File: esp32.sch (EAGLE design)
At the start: 65 parts, among them IC1 PEC11R-4230K-S00243D, IC2 AD8532ARZ, T1 BST82-1, T2 BST82-1, T3 BST82-1, U1 ESP32-WROOM-32D, X1 JST-XH-02-PIN-LONG-PAD, X2 JST-XH-03-PIN-LONG-PAD, X3 JST-XH-03-PIN-LONG-PAD, X4 JST-XH-02-PIN-LONG-PAD

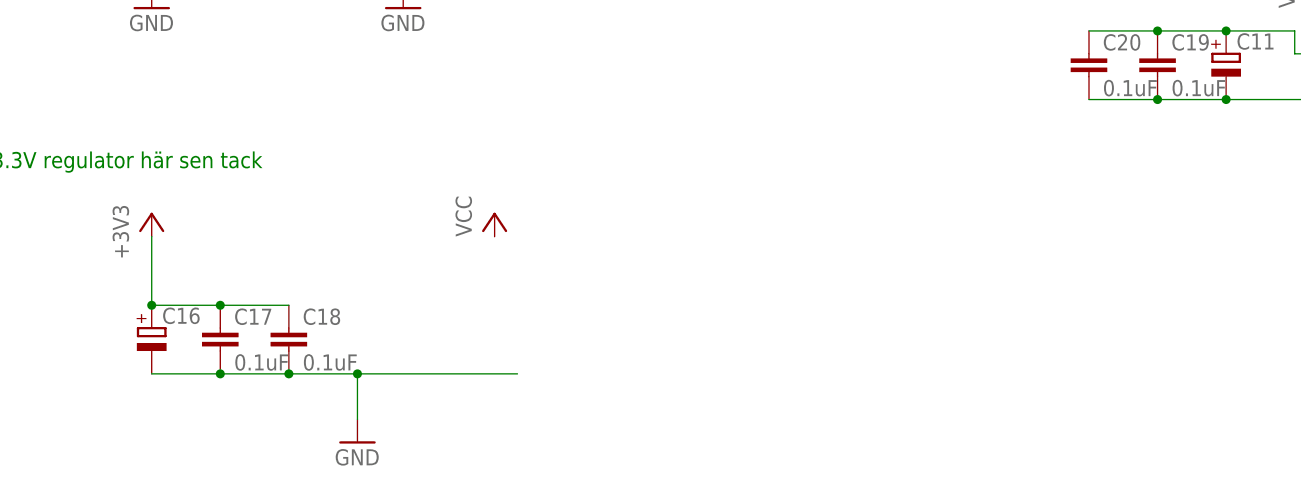
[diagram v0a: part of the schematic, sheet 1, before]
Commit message: Delade upp i lite olika plan. Rätta footprints för kondingar och 3.3V regulator.
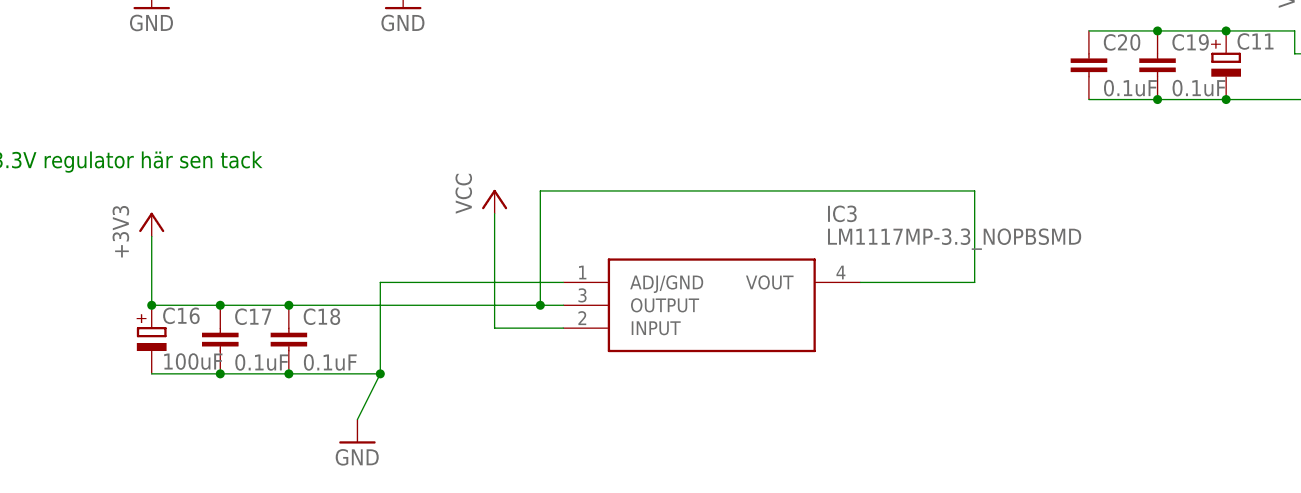
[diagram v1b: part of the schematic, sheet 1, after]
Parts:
- added IC3: LM1117MP-3.3_NOPBSMD, Test:LM1117MP-3.3_NOPBSMD
- C11, C14, C22: device rcl:CPOL-EU140CLH-0810 -> rcl:CPOL-EU153CLV-0605
- C16: value (none) -> 100uF; device rcl:CPOL-EU140CLH-0810 -> rcl:CPOL-EU153CLV-0605
- C7, C8: device rcl:C-EUC0603 -> rcl:CPOL-EU153CLV-0505
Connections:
- net +3V3: now also IC3.OUTPUT, IC3.VOUT
- net AUDIO_FROM_ESP32: now also C8.+; no longer C8.1
- net GND: now also C7.-, IC3.ADJ/GND; no longer C7.2
- net N$10: now also C7.+; no longer C7.1
- net N$4: now also C8.-; no longer C8.2
- net VCC: now also IC3.INPUT

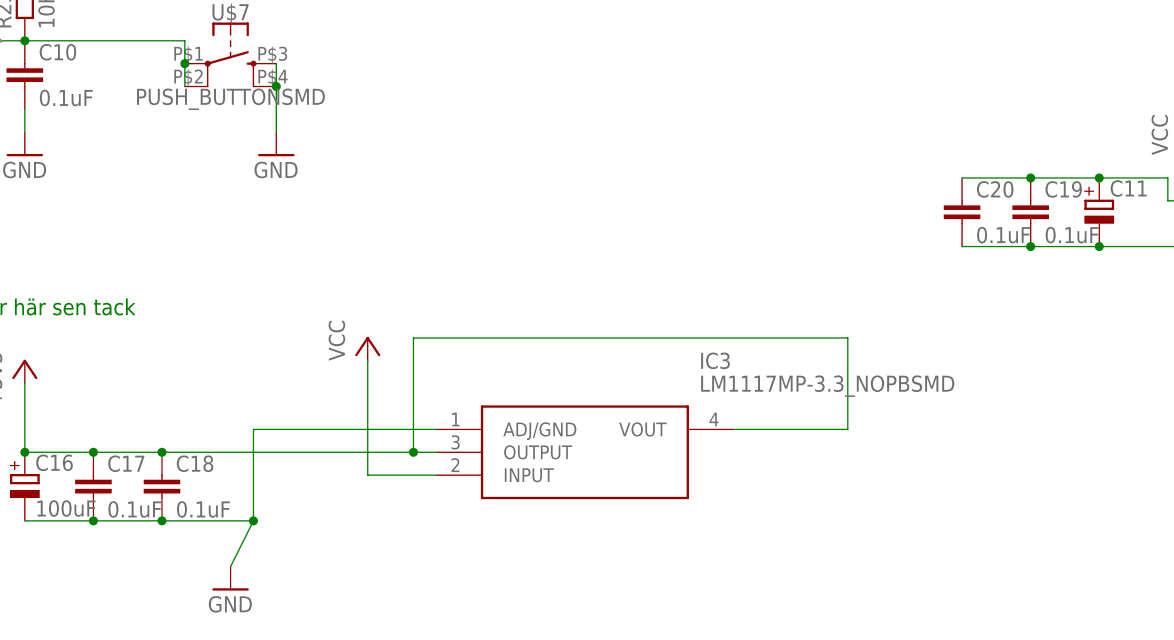
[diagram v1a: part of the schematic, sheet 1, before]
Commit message: Delad upp jordplanet till flera beroende på signal, hört att det ska vara bra att ta bort loopar i jorden.
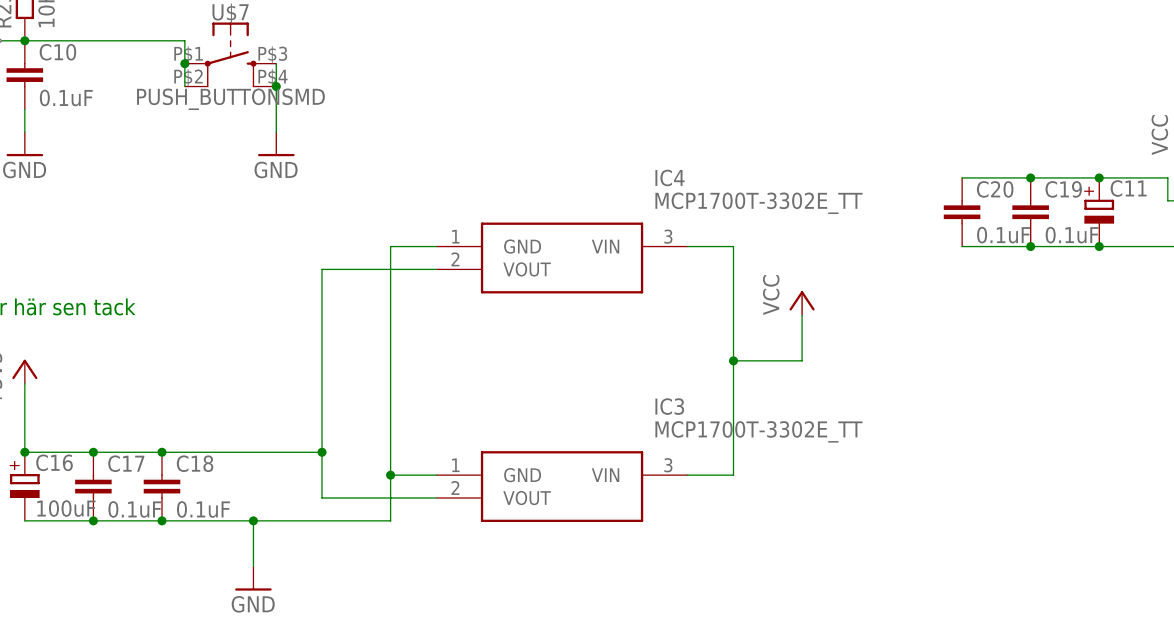
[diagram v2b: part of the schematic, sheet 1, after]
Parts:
- added IC4: MCP1700T-3302E_TT, Test:MCP1700T-3302E_TT
- IC3: value LM1117MP-3.3_NOPBSMD -> MCP1700T-3302E_TT; device Test:LM1117MP-3.3_NOPBSMD -> Test:MCP1700T-3302E_TT
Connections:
- net +3V3: now also IC4.VOUT; no longer IC3.OUTPUT
- net GND: now also IC3.GND, IC4.GND; no longer IC3.ADJ/GND
- net VCC: now also IC3.VIN, IC4.VIN; no longer IC3.INPUT

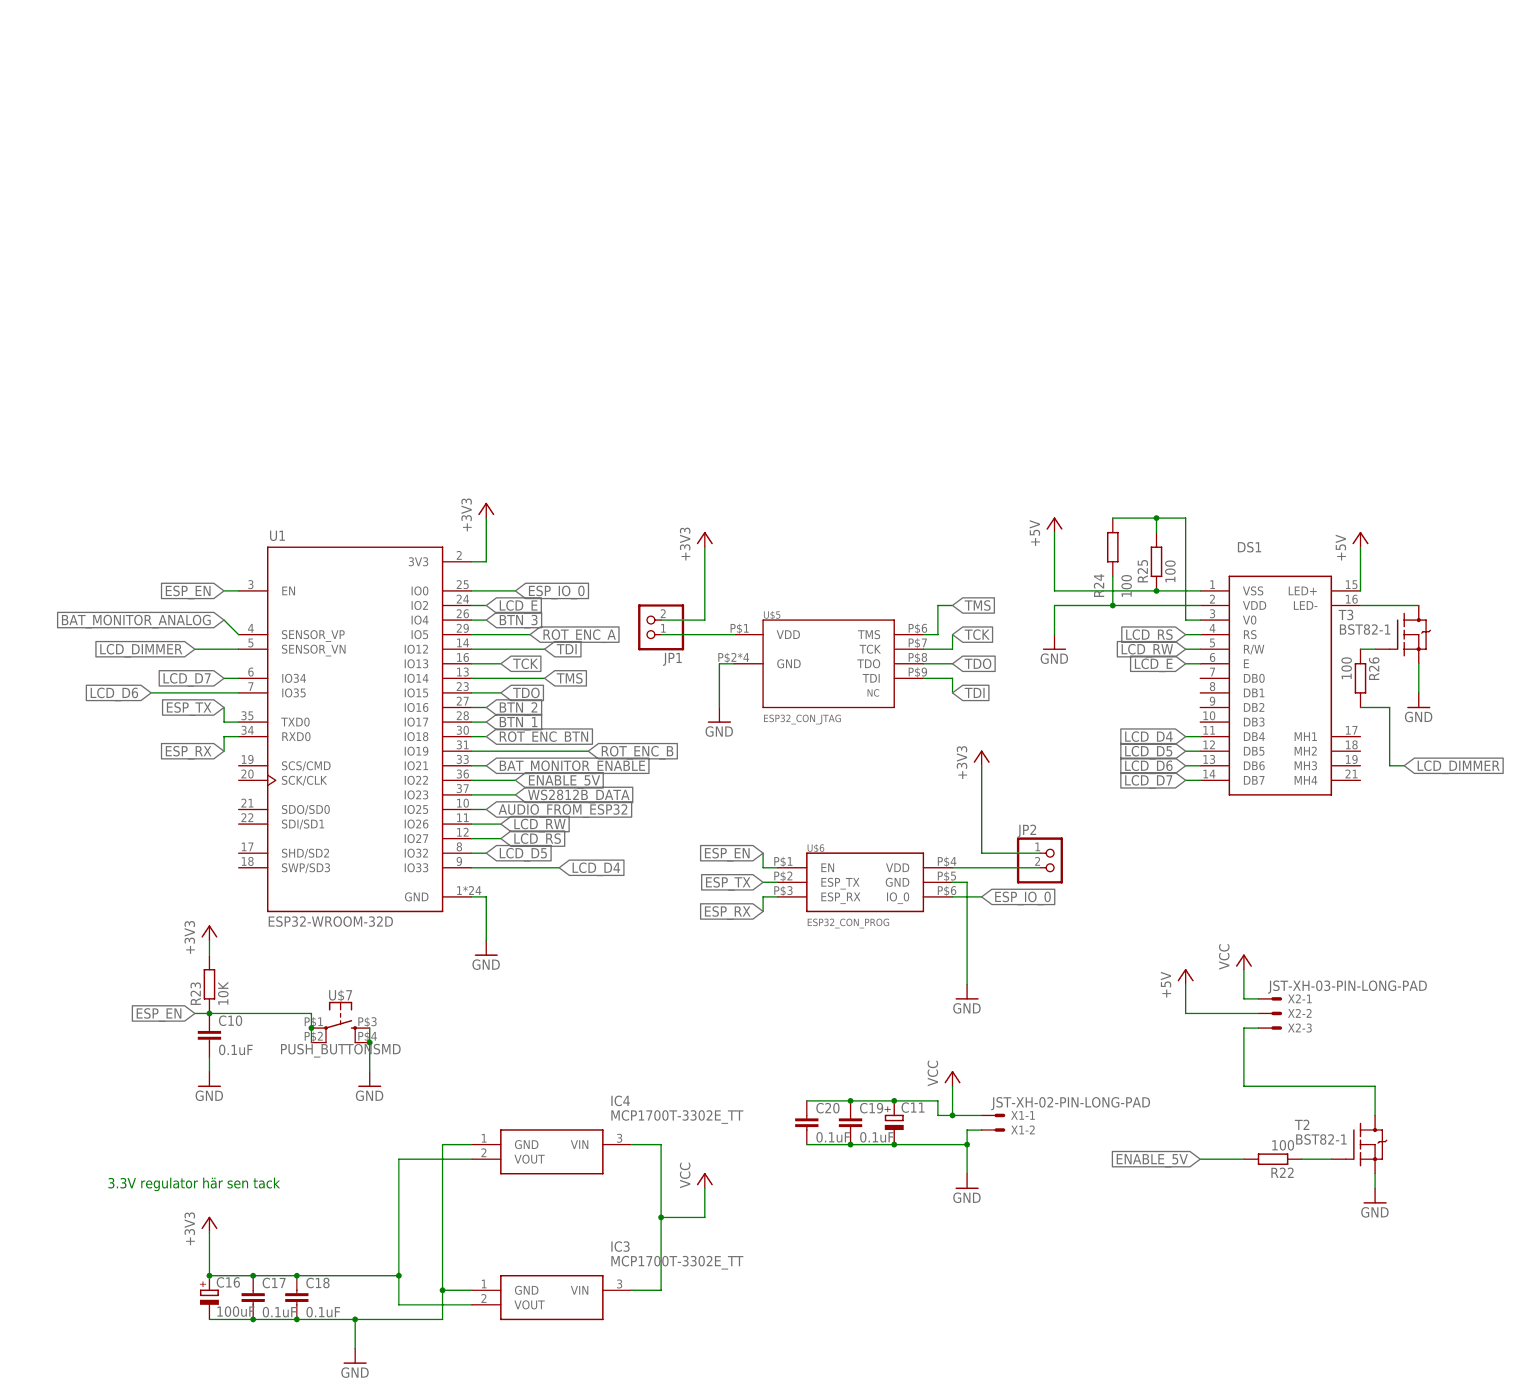
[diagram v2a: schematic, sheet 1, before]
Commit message: Nya upplägget fungera bra, kanske till och med mindre vior än innan, får in mer på mindre plats också. Kommit kanske 70% nu.
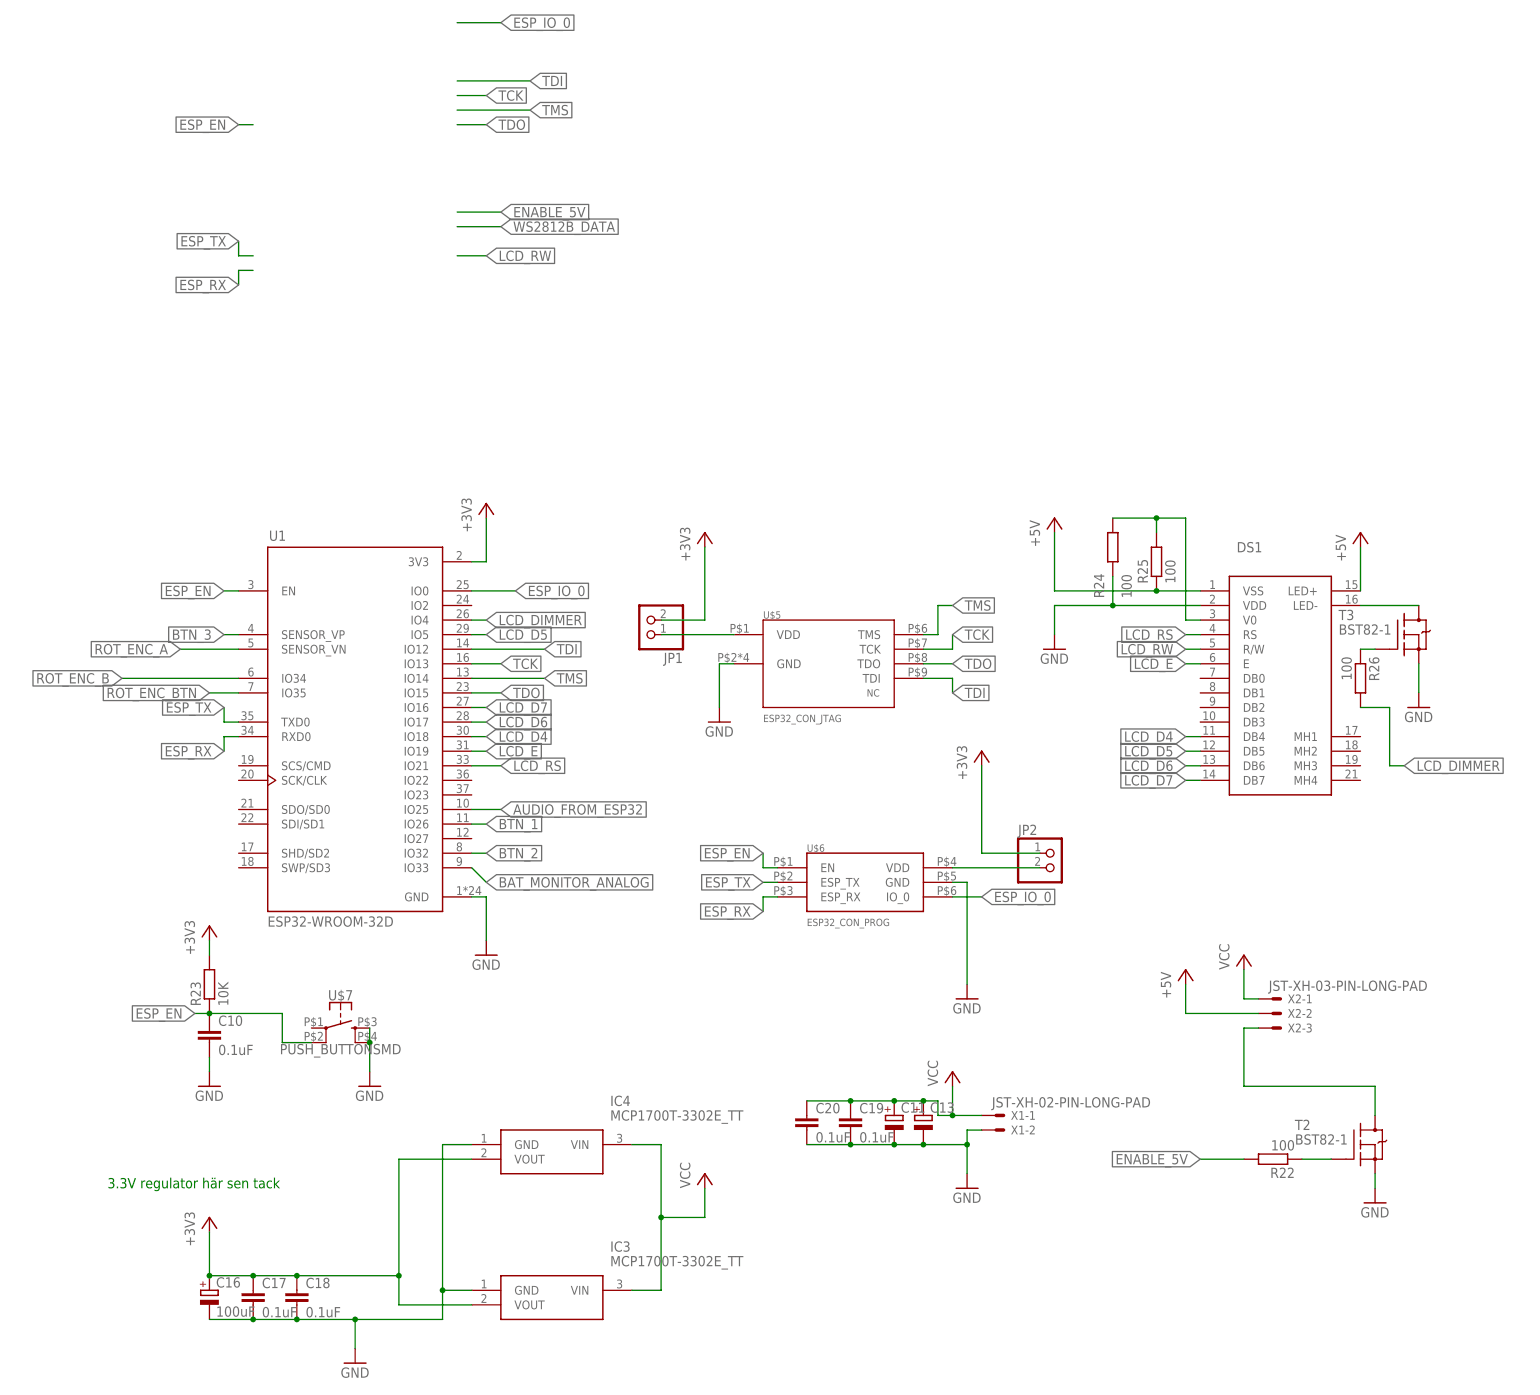
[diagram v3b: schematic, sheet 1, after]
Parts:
- added C12: 270uF, rcl:CPOL-EU153CLV-0605
- added C13: (no value), rcl:CPOL-EU153CLV-0505
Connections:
- net BAT_MONITOR_ANALOG: now also U1.IO33; no longer U1.SENSOR_VP
- net BAT_MONITOR_ENABLE: no longer U1.IO21
- net BTN_1: now also U1.IO26; no longer U1.IO17
- net BTN_2: now also U1.IO32; no longer U1.IO16
- net BTN_3: now also U1.SENSOR_VP; no longer U1.IO4
- net ENABLE_5V: no longer U1.IO22
- net ESP_EN: no longer U$7.1
- net GND: now also C13.-
- net LCD_D4: now also U1.IO18; no longer U1.IO33
- net LCD_D5: now also U1.IO5; no longer U1.IO32
- net LCD_D6: now also U1.IO17; no longer U1.IO35
- net LCD_D7: now also U1.IO16; no longer U1.IO34
- net LCD_DIMMER: now also U1.IO4; no longer U1.SENSOR_VN
- net LCD_E: now also U1.IO19; no longer U1.IO2
- net LCD_RS: now also U1.IO21; no longer U1.IO27
- net LCD_RW: no longer U1.IO26
- net N$14: now also C12.+
- net ROT_ENC_A: now also U1.SENSOR_VN; no longer U1.IO5
- net ROT_ENC_B: now also U1.IO34; no longer U1.IO19
- net ROT_ENC_BTN: now also U1.IO35; no longer U1.IO18
- net SPEAKER_OUT: now also C12.-
- net VCC: now also C13.+
- net WS2812B_DATA: no longer U1.IO23

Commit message: All är routat, behövs dock nya avtryck för JST och skämen.
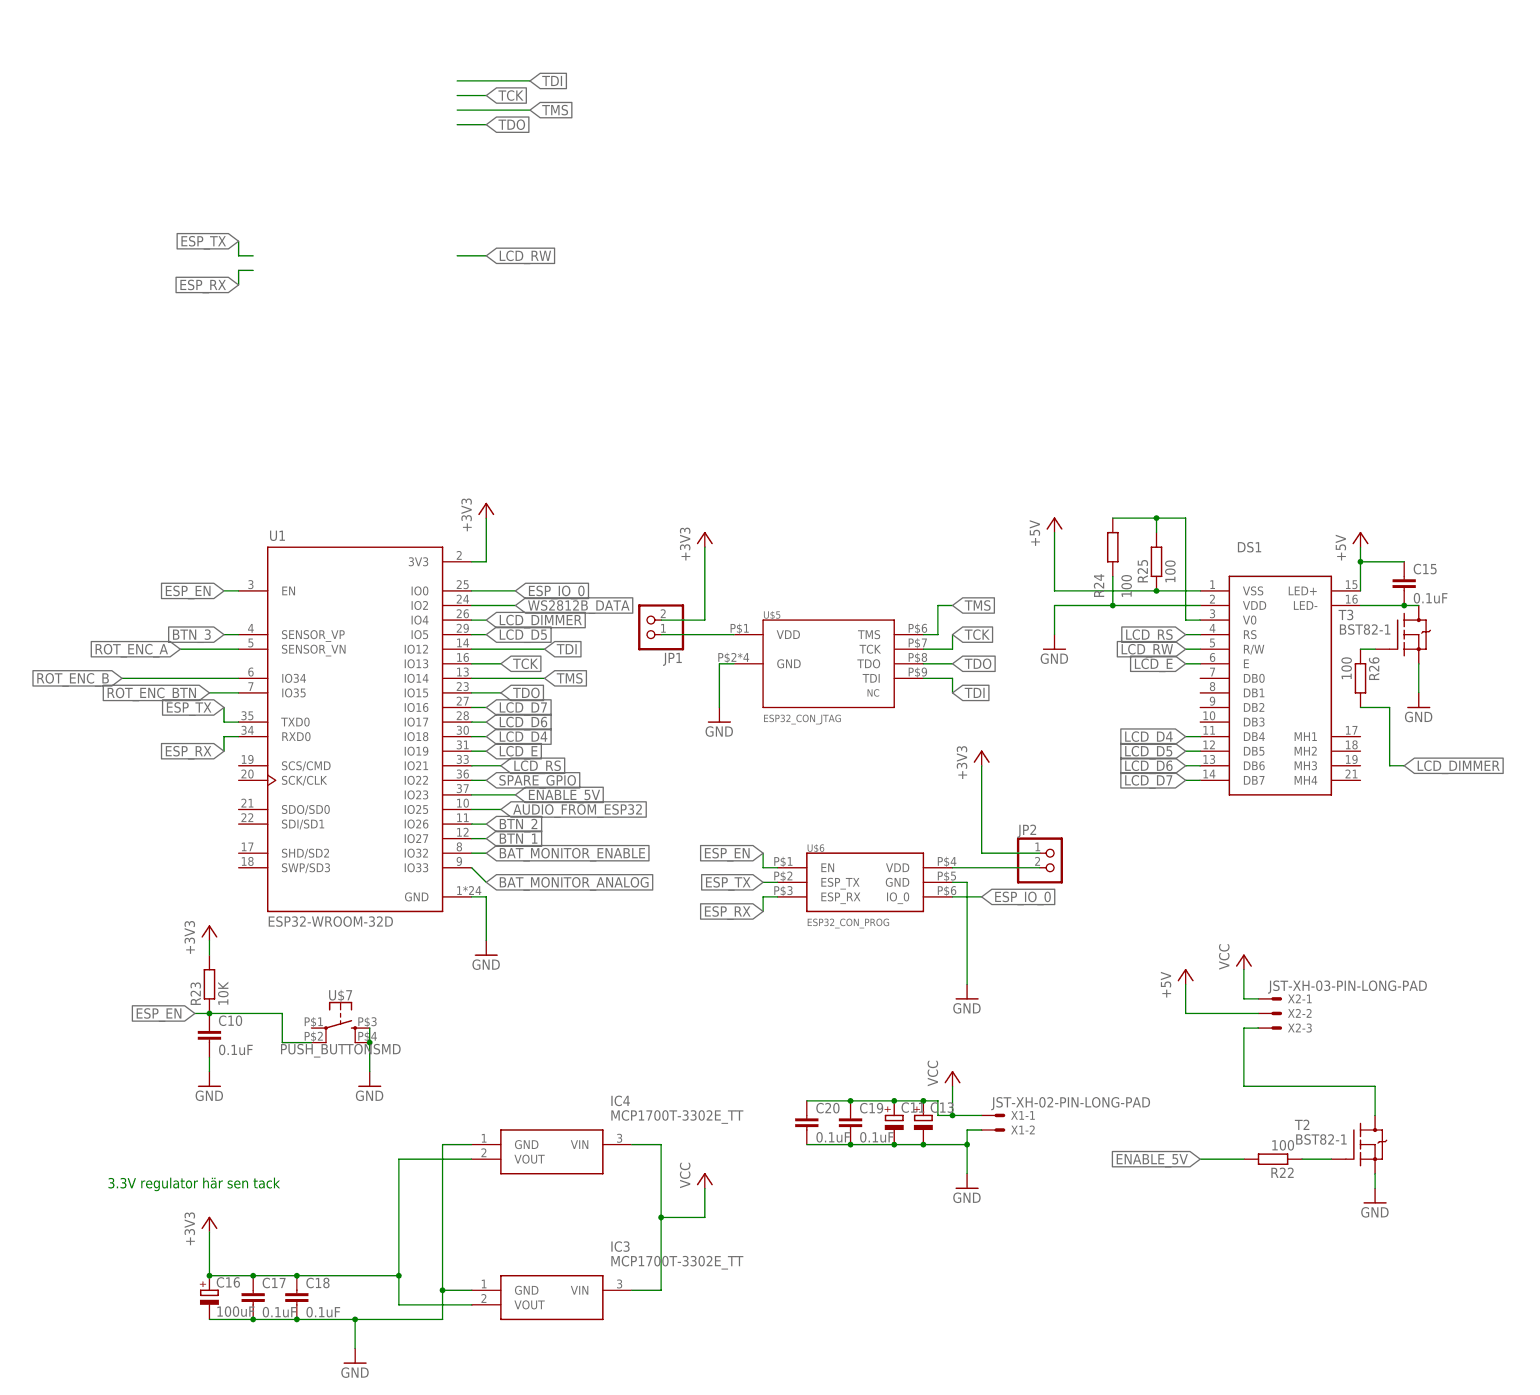
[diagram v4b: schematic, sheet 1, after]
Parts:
- added C15: 0.1uF, rcl:C-EUC0603
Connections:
- new net SPARE_GPIO: U1.IO22
- net +5V: now also C15.1
- net BAT_MONITOR_ENABLE: now also U1.IO32
- net BTN_1: now also U1.IO27; no longer U1.IO26
- net BTN_2: now also U1.IO26; no longer U1.IO32
- net ENABLE_5V: now also U1.IO23
- net N$18: now also C15.2
- net WS2812B_DATA: now also U1.IO2
